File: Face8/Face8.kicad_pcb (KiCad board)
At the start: 2 copper layers, 99.1 x 99.1 mm, 23 parts, among them J1 Conn_01x02, J2 Conn_01x02, J3 Conn_02x04_Counter_Clockwise, J4 Conn_02x04_Counter_Clockwise, J5 Conn_01x02, SW1 SW_Push, SW2 SW_Push, SW3 SW_Push, SW4 SW_Push

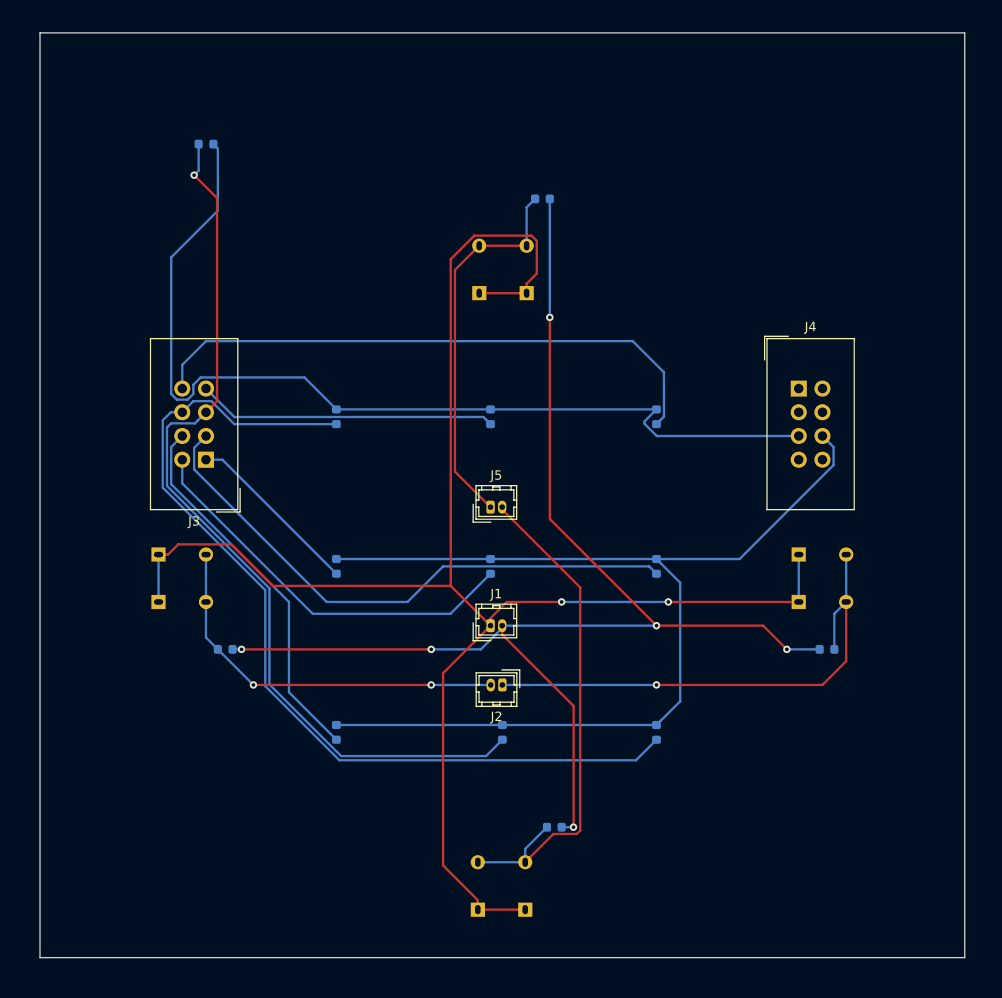
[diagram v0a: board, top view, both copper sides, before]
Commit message: Changed to multiple AS1105 for LED drivers
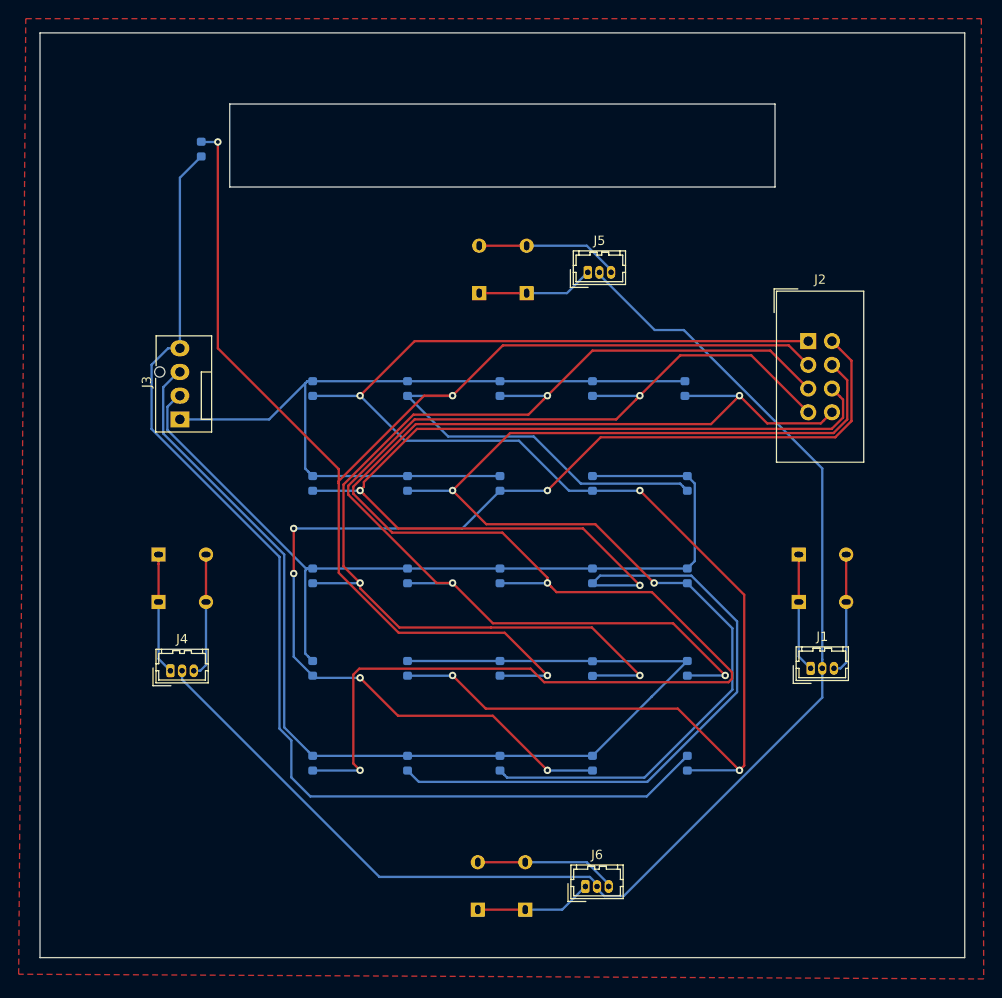
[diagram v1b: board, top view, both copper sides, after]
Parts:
- removed R1, R2, R3, R4: 10k, Resistor_SMD:R_0603_1608Metric
- added D10: LED, LED_SMD:LED_0603_1608Metric, B.Cu at (170.9, 95.2)
- added D11: LED, LED_SMD:LED_0603_1608Metric, B.Cu at (130.8, 105.2)
- added D12: LED, LED_SMD:LED_0603_1608Metric, B.Cu at (141.0, 105.2)
- added D13: LED, LED_SMD:LED_0603_1608Metric, B.Cu at (150.9, 105.2)
- added D14: LED, LED_SMD:LED_0603_1608Metric, B.Cu at (160.8, 105.2)
- added D15: LED, LED_SMD:LED_0603_1608Metric, B.Cu at (170.9, 105.2)
- added D16: LED, LED_SMD:LED_0603_1608Metric, B.Cu at (130.8, 115.1)
- added D17: LED, LED_SMD:LED_0603_1608Metric, B.Cu at (141.0, 115.1)
- added D18: LED, LED_SMD:LED_0603_1608Metric, B.Cu at (150.9, 115.1)
- added D19: LED, LED_SMD:LED_0603_1608Metric, B.Cu at (160.8, 115.1)
- added D20: LED, LED_SMD:LED_0603_1608Metric, B.Cu at (170.9, 115.1)
- added D21: LED, LED_SMD:LED_0603_1608Metric, B.Cu at (130.8, 125.2)
- added D22: LED, LED_SMD:LED_0603_1608Metric, B.Cu at (141.0, 125.2)
- added D23: LED, LED_SMD:LED_0603_1608Metric, B.Cu at (150.9, 125.2)
- added D24: LED, LED_SMD:LED_0603_1608Metric, B.Cu at (160.8, 125.2)
- added D9: LED, LED_SMD:LED_0603_1608Metric, B.Cu at (160.8, 95.2)
- added J6: Conn_01x03_Male, Connector_Hirose:Hirose_DF13-03P-1.25DSA_1x03_P1.25mm_Vertical, F.Cu at (160.0, 138.4)
- J1, J5: value Conn_01x02 -> Conn_01x03_Male; footprint Connector_Hirose:Hirose_DF13-02P-1.25DSA_1x02_P1.25mm_Vertical -> Connector_Hirose:Hirose_DF13-03P-1.25DSA_1x03_P1.25mm_Vertical
- J2: value Conn_01x02 -> Conn_02x04_Odd_Even; footprint Connector_Hirose:Hirose_DF13-02P-1.25DSA_1x02_P1.25mm_Vertical -> Connector_IDC:IDC-Header_2x04_P2.54mm_Vertical
- J3: value Conn_02x04_Counter_Clockwise -> Conn_01x04_Male; footprint Connector_IDC:IDC-Header_2x04_P2.54mm_Vertical -> Connector:FanPinHeader_1x04_P2.54mm_Vertical
- J4: value Conn_02x04_Counter_Clockwise -> Conn_01x03_Male; footprint Connector_IDC:IDC-Header_2x04_P2.54mm_Vertical -> Connector_Hirose:Hirose_DF13-03P-1.25DSA_1x03_P1.25mm_Vertical
- moved D25 84.0 mm to (170.9, 125.2), turned to 270 degrees
- moved J4 73.8 mm to (115.6, 115.3)
- moved J2 49.3 mm to (183.9, 80.0), turned to 0 degrees
- moved J1 34.6 mm to (184.2, 115.1)
- moved D26 32.1 mm to (118.9, 59.4), turned to 90 degrees
- moved D8 31.5 mm to (150.9, 95.2)
- moved D7 28.5 mm to (141.0, 95.2)
- moved J5 27.2 mm to (160.3, 72.6)
- moved D2 26.8 mm to (141.0, 85.1)
- moved D6 26.8 mm to (130.8, 95.2)
- moved D3 25.9 mm to (150.9, 85.1)
- moved D4 22.0 mm to (160.8, 85.1)
- moved D5 19.3 mm to (170.7, 85.1)
- moved D1 19.3 mm to (130.8, 85.1)
- moved J3 5.14 mm to (116.6, 88.4), turned to 90 degrees
- renumbered D3 to D1, D4 to D2, D1 to D25, D2 to D26, D5 to D3, D6 to D4, D7 to D5, D8 to D6, D9 to D7, D10 to D8
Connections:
- D1 pad 1: DIG4 -> DIG0
- D1 pad 2: SEGG -> SEGA
- D2 pad 1: DIG4 -> DIG0
- D2 pad 2: SEGDP -> SEGB
- D25 pad 1: DIG4 -> DIG3
- D25 pad 2: SEGE -> SEGA
- D26 pad 1: DIG4 -> DIG3
- D26 pad 2: SEGF -> SEGB
- D3 pad 1: DIG5 -> DIG0
- D3 pad 2: SEGA -> SEGC
- D4 pad 1: DIG5 -> DIG0
- D4 pad 2: SEGB -> SEGD
- D5 pad 1: DIG5 -> DIG0
- D5 pad 2: SEGC -> SEGE
- D6 pad 1: DIG5 -> DIG0
- D6 pad 2: SEGD -> SEGF
- D7 pad 1: DIG5 -> DIG0
- D7 pad 2: SEGE -> SEGG
- D8 pad 1: DIG5 -> DIG0
- D8 pad 2: SEGF -> SEGDP
- J2 pad 1: GPIO0 -> SEGA
- J2 pad 2: GPIO1 -> SEGDP
- J3 pad 1: SEGA -> DIG0
- J3 pad 2: SEGB -> DIG1
- J3 pad 3: SEGC -> DIG2
- J3 pad 4: SEGD -> DIG3
- J4 pad 1: DIG0 -> GND
- J4 pad 2: DIG1 -> 3.3V
- J4 pad 3: DIG2 -> GPIO1
- J5 pad 1: GPIO2 -> GND
- J5 pad 2: GPIO3 -> 3.3V
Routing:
- net SEGA: track 19.0 -> 169.9 mm, vias 0 -> 4
- net SEGB: track 43.1 -> 181.8 mm, vias 0 -> 3
- net GND: track 180.1 -> 50.8 mm, vias 2 -> 0
- net DIG2: track 0.00 -> 122.9 mm
- net DIG3: track 0.00 -> 120.7 mm
- net DIG5: track 115.2 -> 0.00 mm
- net DIG4: track 103.4 -> 0.00 mm
- net DIG1: track 0.00 -> 97.2 mm
- net SEGG: track 32.1 -> 128.6 mm, vias 0 -> 2
- net DIG0: track 0.00 -> 86.1 mm
- net SEGD: track 40.4 -> 120.9 mm, vias 0 -> 3
- net SEGE: track 96.2 -> 175.5 mm, vias 1 -> 3
- net SEGF: track 99.6 -> 168.5 mm, vias 0 -> 2
- net SEGDP: track 62.5 -> 124.7 mm, vias 0 -> 5
- net SEGC: track 61.4 -> 118.4 mm, vias 0 -> 3
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- added copper zone on F.Cu, net GND
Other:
- outline, holes or cut-outs redrawn
